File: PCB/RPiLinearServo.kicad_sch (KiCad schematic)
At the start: 14 parts, among them J1 Conn_01x03_Pin, J2 Conn_02x02_Odd_Even, U1 TMC2209_SILENTSTEPSTICK, U2 RP2040-ZERO, U3 DRV5055A3xDBZxQ1

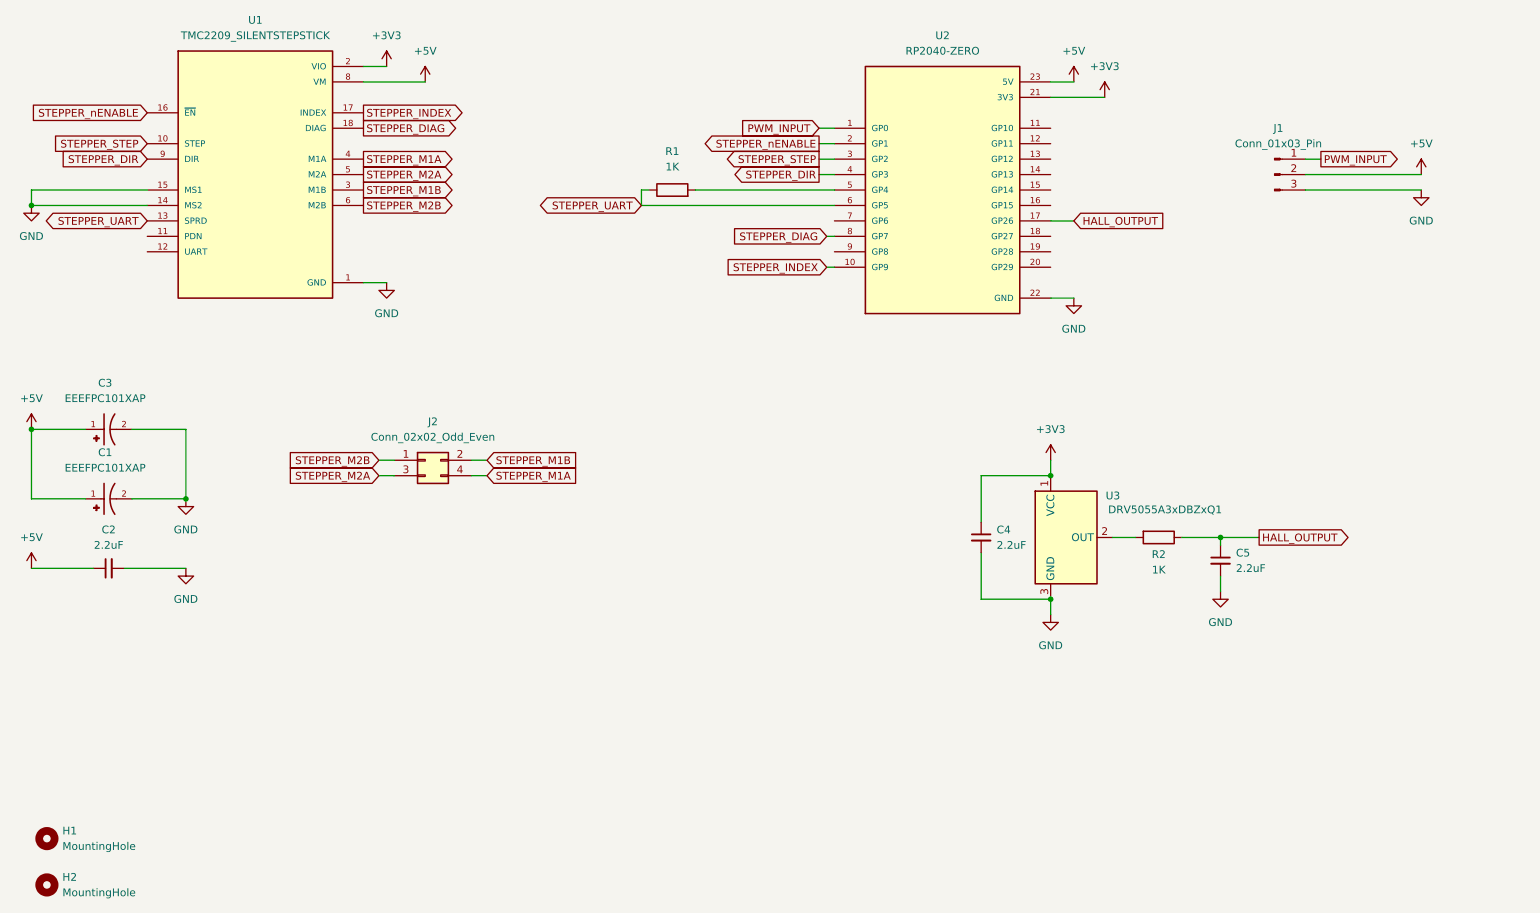
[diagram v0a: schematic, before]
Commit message: Add ESD protection on pwm input, fix wrapping bug in nvm storage logic
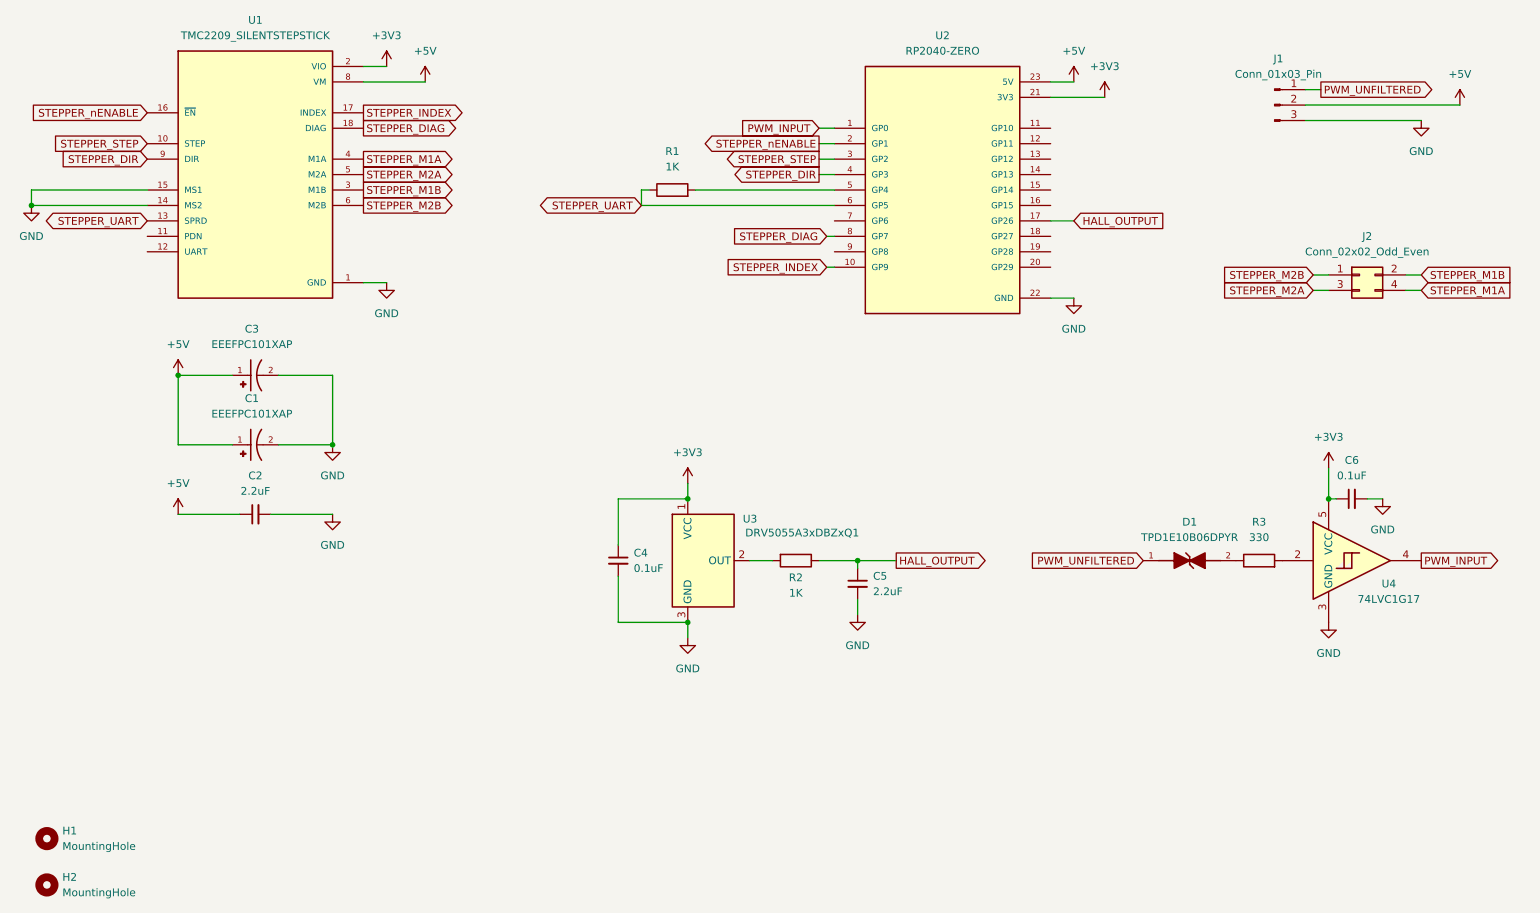
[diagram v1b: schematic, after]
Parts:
- added C6: 0.1uF, Capacitor_SMD:C_0402_1005Metric_Pad0.74x0.62mm_HandSolder, symbol Device:C_Small
- added D1: TPD1E10B06DPYR, Diode_SMD:D_0402_1005Metric_Pad0.77x0.64mm_HandSolder, symbol TPD1E10B06DPYR:TPD1E10B06DPYR
- added R3: 330, Resistor_SMD:R_0603_1608Metric_Pad0.98x0.95mm_HandSolder, symbol Device:R
- added U4: 74LVC1G17, Package_TO_SOT_SMD:SOT-23-5_HandSoldering, symbol 74xGxx:74LVC1G17
- C4: value 2.2uF -> 0.1uF; footprint Capacitor_SMD:C_0805_2012Metric_Pad1.18x1.45mm_HandSolder -> Capacitor_SMD:C_0402_1005Metric_Pad0.74x0.62mm_HandSolder
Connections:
- net +3V3: now also C6.1, U4.5 (VCC)
- net GND: now also C6.2, U4.3 (GND)
- net PWM_INPUT: now also U4.4; no longer J1.1 (Pin_1)
- new net: R3.2, U4.2
- new net: D1.2, R3.1
- new net PWM_UNFILTERED: D1.1, J1.1 (Pin_1)
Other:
- moved on the sheet: C1, C2, C3, C4, C5, J1, J2, R2, U3

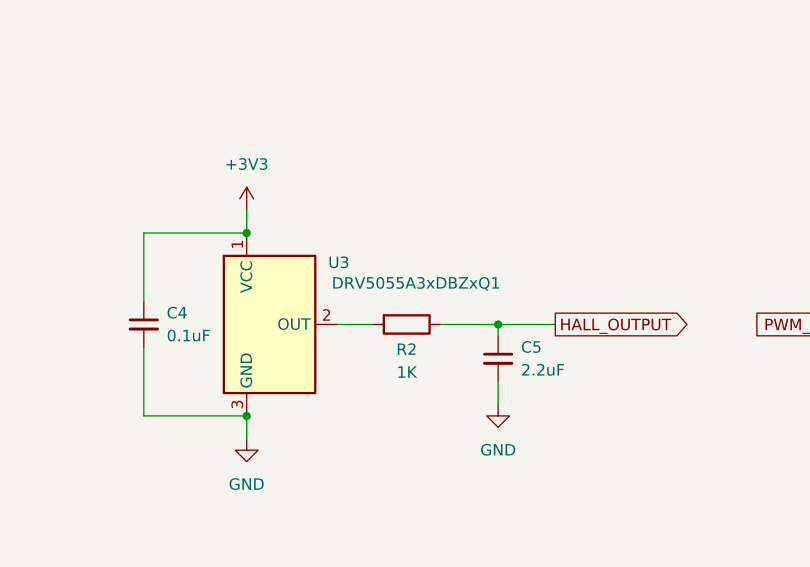
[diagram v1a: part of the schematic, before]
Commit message: Refactor firmware, update PCB schematic, and add per-directory READMEs
Firmware:
- Add hall sensor driver, servo loop, hall verification, and position store
- Move config/NVM storage to storage/ directory, add CRC32
- Add status LED UI module, flash map header
- Refactor stepgen, PWM input, TMC2209 driver, WS2812, homing, CLI
- Add composite USB (CDC+MSC) with virtual FAT12 config drive

PCB:
- Update KiCad schematic

Documentation:
- Rewrite root README as project entry point with feature overview
- Add Firmware/RPiLinearServo/README.md (architecture, build, modules)
- Add PCB/README.md (BOM, GPIO map, sourcing, manufacturing outputs)
- Add Mechanical/README.md (mount variants, print settings, assembly)
- Add project renders (front_render.png, rear_render.png)
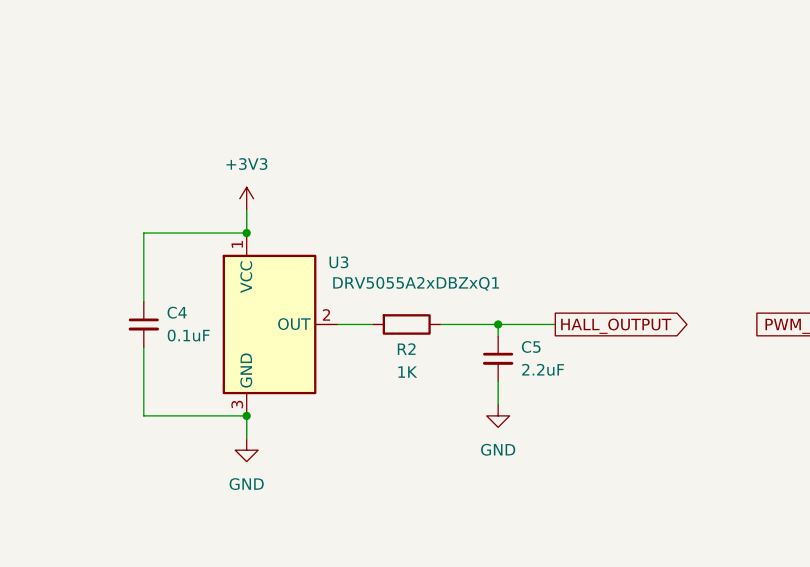
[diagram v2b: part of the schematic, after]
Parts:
- U3: value DRV5055A3xDBZxQ1 -> DRV5055A2xDBZxQ1
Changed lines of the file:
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@@
 			)
 		)
-		(property "Value" "DRV5055A3xDBZxQ1"
+		(property "Value" "DRV5055A2xDBZxQ1"
 			(at 165.354 114.808 0)
 			(effects
